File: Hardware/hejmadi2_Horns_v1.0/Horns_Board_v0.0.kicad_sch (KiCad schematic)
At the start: 4 parts, among them J1 Conn_01x03, J2 Conn_01x02, J3 Conn_01x02, J4 Conn_01x02

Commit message: Horns Board schematic
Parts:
- added C1, C2, C3, C4: 0.1µF, symbol device:C
- added C5, C6: 1uF, symbol device:C
- added C7, C8: 10uF, symbol device:C
- added C9: 100uF, symbol device:C_Polarized
- added D1: US2DA, Diode_SMD:D_SMA, symbol Diode:US2DA
- added F1: 2A, symbol device:Fuse
- added Q1: IRFR010PBF, symbol device:Q_NMOS_GDS
- added R1: 1k, symbol Device:R_US
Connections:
- net +24V: now also C2.1, C3.1, C4.1, C5.1, C6.1, C7.1, C8.1, C9.1
- net GND: now also C1.2, C2.2, C3.2, C4.2, C5.2, C6.2, C7.2, C8.2, C9.2, Q1.3 (S)
- net HORN_CTL: now also Q1.1 (G), R1.1
- net HORN_IN: now also F1.1
- net at J4.2 (Pin_2): now also D1.2 (A); no longer J3.1 (Pin_1)
- new net: C1.1, R1.2
- new net: D1.1 (K), J3.1 (Pin_1)
- new net: F1.2, Q1.2 (D)
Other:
- moved on the sheet: J1, J2, J3, J4

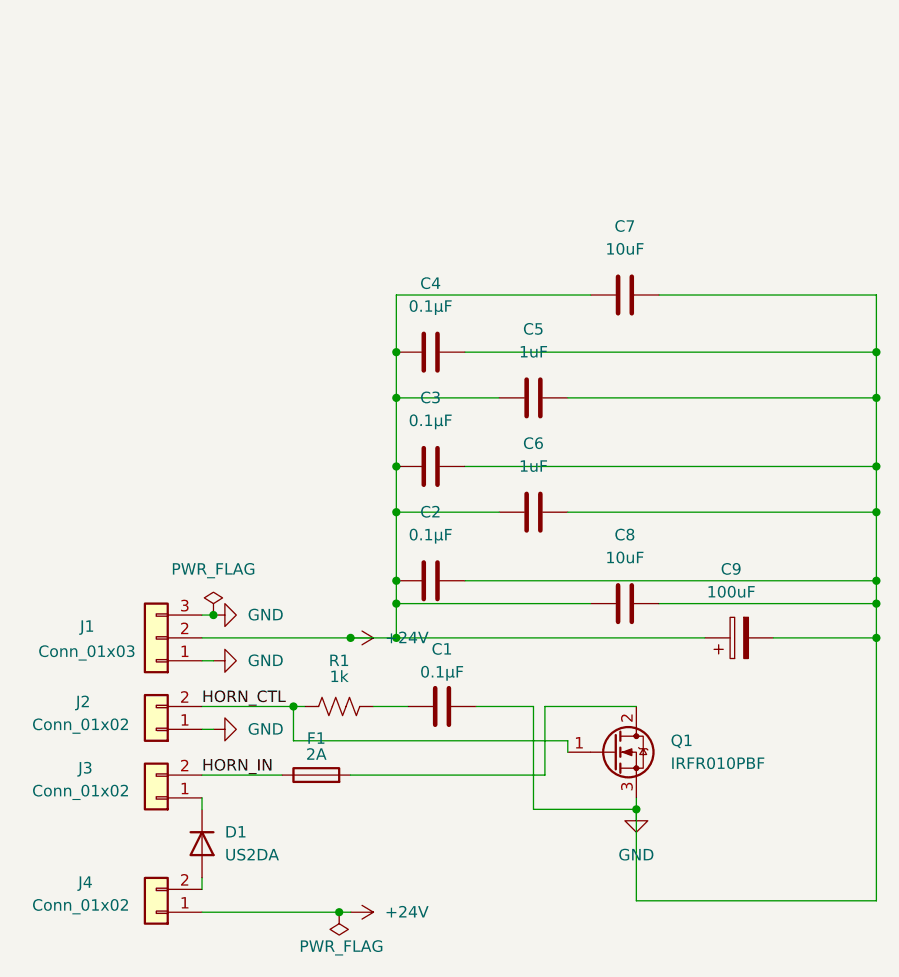
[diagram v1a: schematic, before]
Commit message: Horns Board pcb
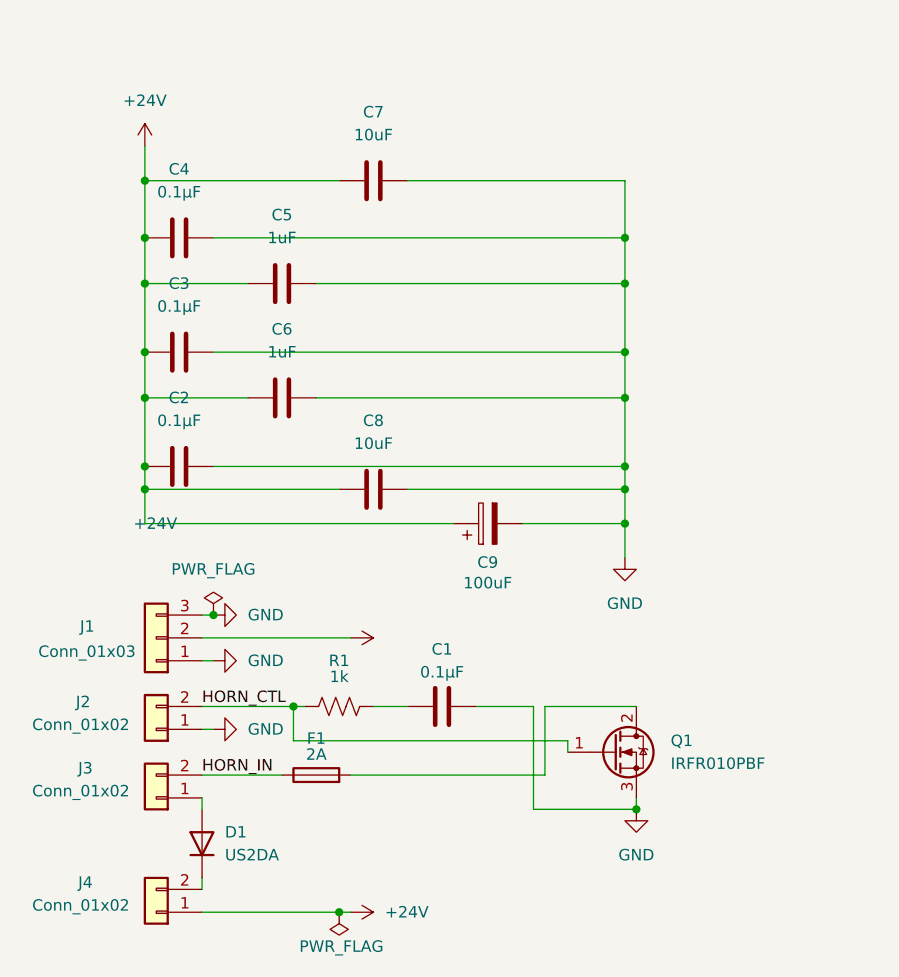
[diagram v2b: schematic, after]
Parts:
- C1, C2, C3, C4, C5, C6, C7, C8, C9: footprint (none) -> Capacitor_SMD:C_0603_1608Metric_Pad1.08x0.95mm_HandSolder
- F1: footprint (none) -> Fuse:Fuse_0603_1608Metric_Pad1.05x0.95mm_HandSolder
- J1: footprint (none) -> Connector_Molex:Molex_Micro-Fit_3.0_43650-0300_1x03_P3.00mm_Horizontal
- J2, J3, J4: footprint (none) -> Connector_Molex:Molex_Micro-Fit_3.0_43650-0200_1x02_P3.00mm_Horizontal
- Q1: footprint (none) -> Package_SON:Fairchild_DualPower33-6_3x3mm
- R1: footprint (none) -> Resistor_SMD:R_0603_1608Metric_Pad0.98x0.95mm_HandSolder
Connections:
- net at J4.2 (Pin_2): now also D1.1 (K); no longer D1.2 (A)
- net at J3.1 (Pin_1): now also D1.2 (A); no longer D1.1 (K)
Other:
- moved on the sheet: C2, C3, C4, C5, C6, C7, C8, C9, D1
